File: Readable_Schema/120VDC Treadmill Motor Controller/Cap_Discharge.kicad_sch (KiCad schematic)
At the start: 11 parts, among them J9 OSTT7020150, Q7 DN2450N8-G, Q8 VOM1271T

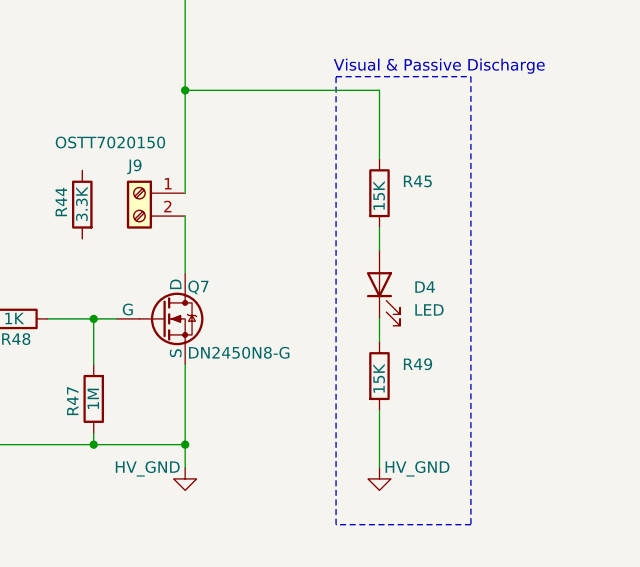
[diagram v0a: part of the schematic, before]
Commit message: -Think we're finished with the schematic (finally) --Upped the LED resistors and added a few more supporting caps for the 3.3v iso supply in the feedback schema
-Started placing footprints
--Now that we're using how air instead of oven I'm not going to try and keep all SMD components on the same side anymore
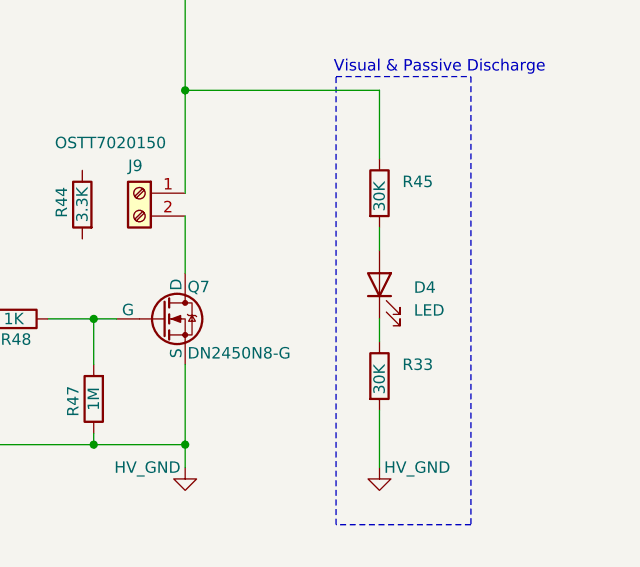
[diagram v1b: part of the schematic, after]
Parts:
- removed R49: 15K, Resistor_SMD:R_1206_3216Metric_Pad1.30x1.75mm_HandSolder, symbol Device:R
- added R33: 30K, Treadmill_Feet:YAG_RSF100_YAG, symbol Device:R
- R45: value 15K -> 30K; footprint Resistor_SMD:R_1206_3216Metric_Pad1.30x1.75mm_HandSolder -> Treadmill_Feet:YAG_RSF100_YAG
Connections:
- net HV_GND: now also R33.2
- net at D4.1 (K): now also R33.1

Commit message: -Changed all footprints from metric to imperial sizing --This meant repositioning everything on the board again.
-Did the first pour for HV GND
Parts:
- C45: footprint Capacitor_SMD:C_0201_0603Metric_Pad0.64x0.40mm_HandSolder -> Capacitor_SMD:C_0603_1608Metric_Pad1.08x0.95mm_HandSolder
- R46, R47, R48: footprint Resistor_SMD:R_0201_0603Metric_Pad0.64x0.40mm_HandSolder -> Resistor_SMD:R_0603_1608Metric_Pad0.98x0.95mm_HandSolder
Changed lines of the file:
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@@
 			)
 		)
-		(property "Footprint" "Resistor_SMD:R_0201_0603Metric_Pad0.64x0.40mm_HandSolder"
+		(property "Footprint" "Resistor_SMD:R_0603_1608Metric_Pad0.98x0.95mm_HandSolder"
 			(at 40.64 107.442 90)
 			(effects
@@
 			)
 		)
-		(property "Footprint" "Resistor_SMD:R_0201_0603Metric_Pad0.64x0.40mm_HandSolder"
+		(property "Footprint" "Resistor_SMD:R_0603_1608Metric_Pad0.98x0.95mm_HandSolder"
 			(at 117.348 115.57 90)
 			(effects
@@
 			)
 		)
-		(property "Footprint" "Resistor_SMD:R_0201_0603Metric_Pad0.64x0.40mm_HandSolder"
+		(property "Footprint" "Resistor_SMD:R_0603_1608Metric_Pad0.98x0.95mm_HandSolder"
 			(at 106.68 104.902 90)
 			(effects
@@
 			)
 		)
-		(property "Footprint" "Capacitor_SMD:C_0201_0603Metric_Pad0.64x0.40mm_HandSolder"
+		(property "Footprint" "Capacitor_SMD:C_0603_1608Metric_Pad1.08x0.95mm_HandSolder"
 			(at 46.6852 118.11 0)
 			(effects
